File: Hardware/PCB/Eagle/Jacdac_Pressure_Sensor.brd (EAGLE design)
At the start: 33.8 x 27.9 mm, 30 parts, among them J1 JACDAC-CONNECTOR, J2 SWD-ADAPTER-, J3 HEADER_MALE-1X07, U1 NCP114ASN330T1G, U2 STM32F042F6P6, U3 BAT54S,235, U4 LPS33HWTR

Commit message: Updated design
Use I2C instead of SPI
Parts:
- J1: value JACDAC-CONNECTOR -> JACDAC_EDGE_CONN-INNIE; device milador:JACDAC-CONNECTOR -> Jacdac:JACDAC-EDGE-CONN-INNIE
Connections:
- removed net N$17: D3.2, FB1.2, J1.P3
- removed net SCK: J3.3, SJ1.1, U2.11, U4.2
- new net J_DATA: D3.2, FB1.2, J1.JD1, J1.JD2, J1.JD3
- new net SCL: J3.3, SJ1.1, U2.17, U4.2
- net GND: now also J1.GND1, J1.GND2, J1.GND3, J1.GND4; no longer J1.P2
- net SDA: now also U2.18; no longer U2.13
- net VCC: now also J1.VDD1, J1.VDD2, J1.VDD3; no longer J1.P1
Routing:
- net SCK: track 34.5 -> 0.00 mm, vias 2 -> 0
- net SCL: track 0.00 -> 29.8 mm, vias 0 -> 2
- net J_DATA: track 0.00 -> 20.4 mm
- net N$17: track 10.8 -> 0.00 mm
- net VCC: track 17.0 -> 24.0 mm
- net SDA: track 33.1 -> 29.1 mm
- net GND: track 14.6 -> 16.4 mm
- net RESET: track 13.1 -> 12.4 mm
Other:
- board size 33.8 x 27.9 mm -> 27.9 x 27.9 mm
- board text added: "SCL"
- board text removed: "SCK"

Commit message: Corrected Capacitor values
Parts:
- C5: value 33pF -> 1uF
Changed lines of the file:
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@@
 <attribute name="NAME" x="14.224" y="8.382" size="0.8128" layer="25" ratio="15" rot="R90" align="bottom-center"/>
 </element>
-<element name="C5" library="milador_SMD" library_urn="urn:adsk.eagle:library:27847482" package="0603" package3d_urn="urn:adsk.eagle:package:29222124/2" value="33pF" x="15.24" y="13.462" smashed="yes">
+<element name="C5" library="milador_SMD" library_urn="urn:adsk.eagle:library:27847482" package="0603" package3d_urn="urn:adsk.eagle:package:29222124/2" value="1uF" x="15.24" y="13.462" smashed="yes">
 <attribute name="NAME" x="12.8524" y="12.9286" size="0.8128" layer="25" font="vector" ratio="15" align="bottom-center"/>
 <attribute name="VALUE" x="13.0302" y="12.4968" size="0.8128" layer="27" font="vector" ratio="15" align="top-center"/>

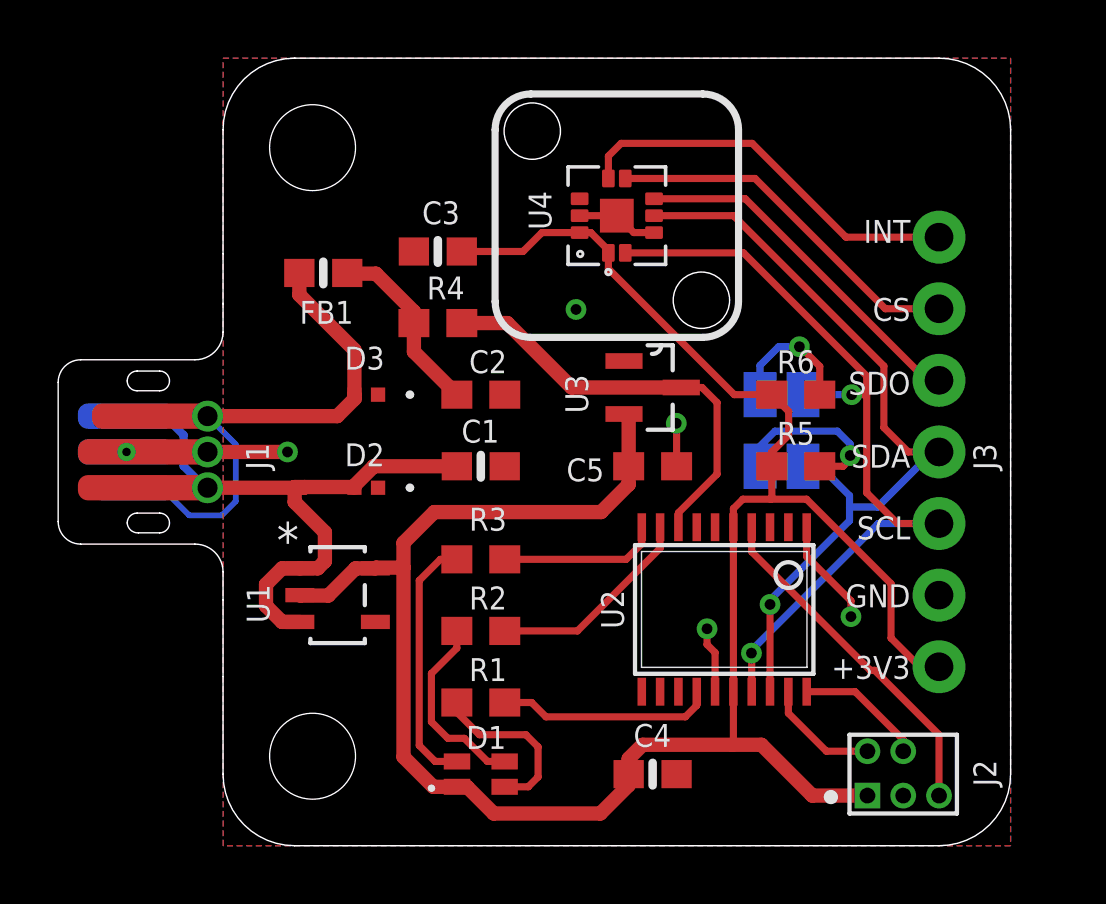
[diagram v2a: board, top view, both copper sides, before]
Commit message: Updated main design
Centering the sensor
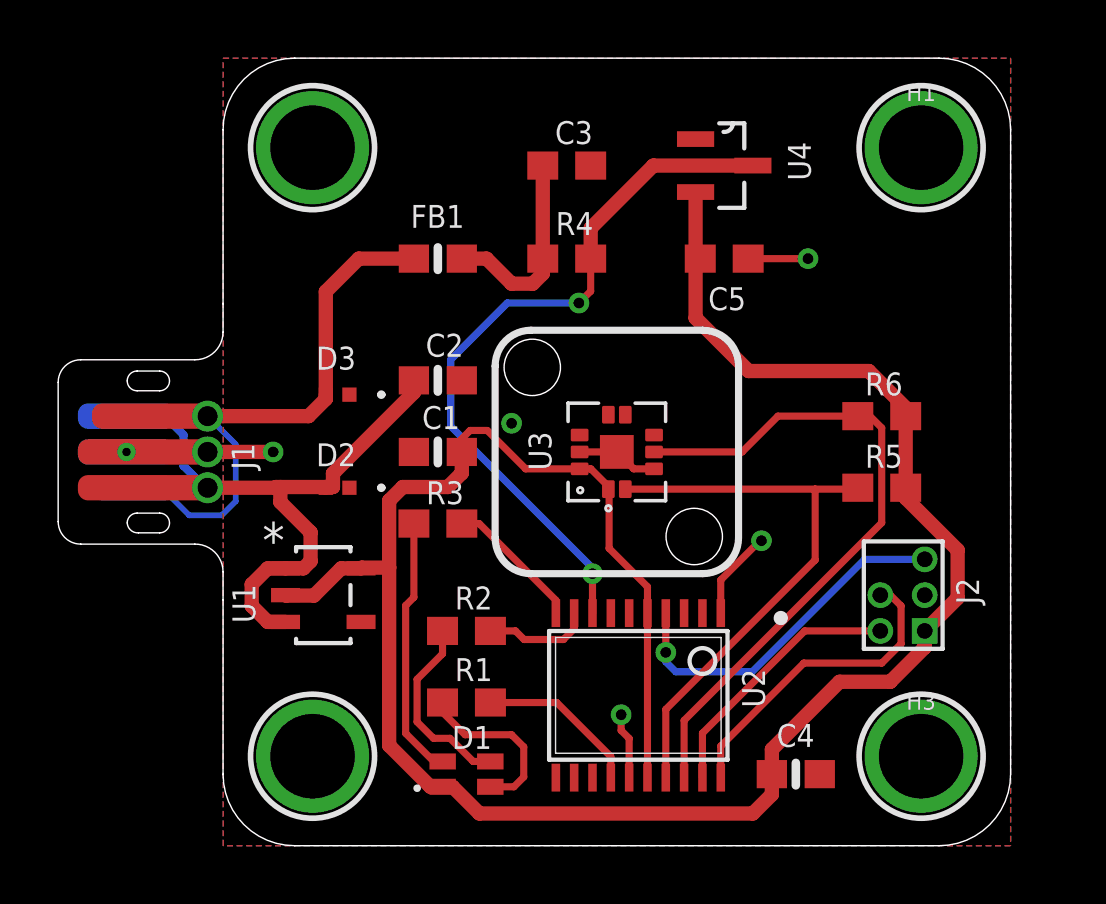
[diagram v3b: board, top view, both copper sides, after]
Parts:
- removed J3: HEADER_MALE-1X07, milador:HEADER_MALE-1X07
- removed SJ1, SJ2: (no value), milador_SMD:SOLDERJUMPER_CLOSEDWIRE
- removed U$1: MILADOR-PIN-NAME-SDA, milador:PIN-SDA
- removed U$2: MILADOR-PIN-NAME-SCK, milador:PIN-SCK
- added H1, H3: MOUNTINGHOLE3.0THIN, milador:MOUNTINGHOLE_3.0_PLATEDTHIN
- C1: value 1uF -> 0.1uF
- C2: value 33pF -> 1uF; device milador_SMD:0603 -> milador_SMD:0603-NO
- C3: value 0.1uF -> 33pF; device milador_SMD:0603-NO -> milador_SMD:0603
- H2, JP3: value STAND-OFF-3.0 -> MOUNTINGHOLE3.0THIN; device milador:STAND-OFF-3.0 -> milador:MOUNTINGHOLE_3.0_PLATEDTHIN
- U3: value BAT54S,235 -> LPS33HWTR; device milador_SMD:SOT23-3 -> milador_SMD:PQFN60P330X330X290-11N
- U4: value LPS33HWTR -> BAT54S,235; device milador_SMD:PQFN60P330X330X290-11N -> milador_SMD:SOT23-3
- moved C5 7.79 mm to (17.8, 20.8)
- moved J2 6.19 mm to (24.9, 7.62), turned to 90 degrees
- moved C3 5.49 mm to (12.2, 24.1), turned to 0 degrees
- moved R4 5.11 mm to (12.2, 20.8)
- moved C4 5.08 mm to (20.3, 2.54)
- moved U2 4.31 mm to (14.7, 5.33)
- moved U4 4.20 mm to (17.8, 24.1), turned to 0 degrees
- moved FB1 4.10 mm to (7.62, 20.8)
- moved R5 3.14 mm to (23.4, 12.7), turned to 0 degrees
- moved R6 3.14 mm to (23.4, 15.2), turned to 0 degrees
- moved U3 2.62 mm to (14.0, 14.0), turned to 90 degrees
- moved R3 1.98 mm to (7.62, 11.4)
- moved C2 1.61 mm to (7.62, 16.5)
- moved C1 1.61 mm to (7.62, 14.0), turned to 180 degrees
- moved D2 1.02 mm to (4.06, 12.7)
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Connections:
- removed net CS: J3.6, U4.6
- removed net INT: J3.7, U4.7
- removed net N$6: R6.1, SJ1.2
- removed net N$7: R5.1, SJ2.2
- removed net SDO: J3.5, U4.5
- net +3V3: now also C1.1, U3.1, U3.10, U4.2; no longer C3.1, J3.1, U3.2, U4.1, U4.10
- net GND: now also U3.3, U3.8, U3.9, U3.EP, U4.1; no longer J3.2, U3.1, U4.3, U4.8, U4.9, U4.EP
- net JD_DATA: now also U4.3; no longer U3.3
- net N$4: now also C3.1; no longer C2.1
- net SCL: now also R5.1, U3.2; no longer J3.3, SJ1.1, U4.2
- net SDA: now also R6.1, U3.4; no longer J3.4, SJ2.1, U4.4
- net VCC: now also C2.1; no longer C1.1
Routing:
- net INT: track 14.1 -> 0.00 mm
- net CS: track 13.0 -> 0.00 mm
- net SDO: track 12.8 -> 0.00 mm
- net JD_DATA: track 15.2 -> 26.0 mm, vias 0 -> 2
- net SCL: track 29.8 -> 20.7 mm, vias 2 -> 0
- net SWCLK: track 4.54 -> 11.3 mm
- net N$7: track 6.04 -> 0.00 mm, vias 1 -> 0
- net SWDIO: track 4.13 -> 9.39 mm
- net SDA: track 29.1 -> 24.1 mm, vias 1 -> 0
- net N$6: track 4.73 -> 0.00 mm, vias 1 -> 0
- net RGB_G: track 7.47 -> 3.81 mm
- net RGB_B: track 7.68 -> 5.81 mm
- net J_DATA: track 20.4 -> 21.5 mm
- net RGB_R: track 5.68 -> 4.92 mm
- net N$4: track 6.51 -> 7.22 mm
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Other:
- outline, holes or cut-outs redrawn
- board text removed: "+3V3"
- board text removed: "CS"
- board text removed: "GND"
- board text removed: "INT"
- board text removed: "SCL"
- board text removed: "SDA"
- board text removed: "SDO"

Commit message: Updated PCB
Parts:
- removed JP3: MOUNTINGHOLE3.0THIN, milador:MOUNTINGHOLE_3.0_PLATEDTHIN
- added H4: MOUNTINGHOLE2.5, milador:MOUNTINGHOLE_2.5_PLATED
- added MMC_LOGO: MMC_LOGO-SM, MMC Eagle:MMC_SMALL_LOGO
- added U$1: JACDAC-DEVICE-LPS33HW, milador:JACDAC-LPS33HW
- H1, H2, H3: value MOUNTINGHOLE3.0THIN -> MOUNTINGHOLE2.5; device milador:MOUNTINGHOLE_3.0_PLATEDTHIN -> milador:MOUNTINGHOLE_2.5_PLATED
- moved H1 30.5 mm to (3.17, 3.17)
- moved H3 21.6 mm to (24.8, 24.8)
- moved LABEL2 15.4 mm to (23.1, 18.6)
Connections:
- net GND: now also H3.P$1, H4.P$1
- net J_DATA: now also H2.P$1
- net VCC: now also H1.P$1
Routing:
- net VCC: track 23.9 -> 29.5 mm
- net J_DATA: track 21.5 -> 26.3 mm
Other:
- board text added: "5V"
- board text added: "GND"
- board text added: "JD"
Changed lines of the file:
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@@
 <setting verticaltext="up"/>
 </settings>
-<grid distance="0.001" unitdist="inch" unit="inch" style="lines" multiple="1" display="yes" altdistance="0.005" altunitdist="inch" altunit="inch"/>
+<grid distance="0.0006" unitdist="inch" unit="inch" style="lines" multiple="1" display="yes" altdistance="0.005" altunitdist="inch" altunit="inch"/>
 <layers>
 <layer number="1" name="Top" color="4" fill="1" visible="yes" active="yes"/>
@@
 </layers>
 <board>
-<fusionsync huburn="a.cGVyc29uYWw6dWUyYWQxOTI2" projecturn="a.cGVyc29uYWw6dWUyYWQxOTI2IzIwMjEwOTEzNDQzNTc2ODA2" f3durn="urn:adsk.wipprod:dm.lineage:uby1OiGsR5OmPWsZuNtneA" pcbguid="" lastpulledtime="" lastsyncedchangeguid="" latestrevisionid="4bb2a5f7-9195-4a02-b50d-8d35879bc375" lastsyncedrevisionid="4bb2a5f7-9195-4a02-b50d-8d35879bc375" lastboardhashguid="187e14e1-9a08-c98b-b799-0e1be3d56bf4" lastpushedtime="2021-09-18T05:05:42Z" linktopcb3d="true"/>
+<fusionsync huburn="a.cGVyc29uYWw6dWUyYWQxOTI2" projecturn="a.cGVyc29uYWw6dWUyYWQxOTI2IzIwMjEwOTEzNDQzNTc2ODA2" f3durn="urn:adsk.wipprod:dm.lineage:uby1OiGsR5OmPWsZuNtneA" pcbguid="" lastpulledtime="" lastsyncedchangeguid="" latestrevisionid="af606afd-fa91-40a1-9cdc-3a86e01ece8c" lastsyncedrevisionid="af606afd-fa91-40a1-9cdc-3a86e01ece8c" lastboardhashguid="dc86e965-abde-f830-b550-b611301090e1" lastpushedtime="2022-03-29T02:43:38Z" linktopcb3d="true"/>
 <plain>
 <wire x1="2.54" y1="27.94" x2="25.4" y2="27.94" width="0.05" layer="20"/>
@@
 <wire x1="9.652" y1="17.018" x2="10.922" y2="18.288" width="0.254" layer="21" curve="-90"/>
 <wire x1="10.922" y1="18.288" x2="17.018" y2="18.288" width="0.254" layer="21"/>
-<circle x="19.7866" y="8.0772" radius="0.127" width="0.254" layer="21"/>
-<circle x="19.7866" y="8.0772" radius="0.127" width="0.254" layer="22"/>
+<circle x="18.5674" y="7.1628" radius="0.127" width="0.254" layer="21"/>
+<circle x="18.5674" y="7.1628" radius="0.127" width="0.254" layer="21"/>
 <wire x1="22.733" y1="10.795" x2="22.733" y2="6.985" width="0.1524" layer="22"/>
 <wire x1="22.733" y1="6.985" x2="25.527" y2="6.985" width="0.1524" layer="22"/>
@@
 <wire x1="25.527" y1="6.985" x2="25.527" y2="10.795" width="0.1524" layer="21"/>
 <wire x1="25.527" y1="10.795" x2="22.733" y2="10.795" width="0.1524" layer="21"/>
+<circle x="24.9428" y="6.2484" radius="0.127" width="0.254" layer="21"/>
+<text x="0.7112" y="21.8948" size="0.8128" layer="21" ratio="15">JD</text>
+<text x="24.9936" y="21.5646" size="0.8128" layer="21" ratio="15">GND</text>
+<text x="0.6604" y="5.4864" size="0.8128" layer="21" ratio="15">5V</text>
+<text x="21.209" y="0.5334" size="0.8128" layer="21" ratio="15">GND</text>
 </plain>
 <attributes>
@@
 </autorouter>
 <elements>
-<element name="JP3" library="milador" library_urn="urn:adsk.eagle:library:12595918" package="MOUNTINGHOLE_3.0_PLATEDTHIN" package3d_urn="urn:adsk.eagle:package:29232285/1" value="MOUNTINGHOLE3.0THIN" x="3.175" y="3.175" smashed="yes">
+<element name="H1" library="milador" library_urn="urn:adsk.eagle:library:12595918" package="MOUNTINGHOLE_2.5_PLATED" package3d_urn="urn:adsk.eagle:package:29232281/2" value="MOUNTINGHOLE2.5" x="3.175" y="3.175" smashed="yes">
 <attribute name="BOM" value="EXCLUDE" x="3.175" y="3.175" size="1.778" layer="27" display="off"/>
 </element>
-<element name="H2" library="milador" library_urn="urn:adsk.eagle:library:12595918" package="MOUNTINGHOLE_3.0_PLATEDTHIN" package3d_urn="urn:adsk.eagle:package:29232285/1" value="MOUNTINGHOLE3.0THIN" x="3.175" y="24.765" smashed="yes">
+<element name="H2" library="milador" library_urn="urn:adsk.eagle:library:12595918" package="MOUNTINGHOLE_2.5_PLATED" package3d_urn="urn:adsk.eagle:package:29232281/2" value="MOUNTINGHOLE2.5" x="3.175" y="24.765" smashed="yes">
 <attribute name="BOM" value="EXCLUDE" x="3.175" y="24.765" size="1.778" layer="27" display="off"/>
 </element>
@@
 </element>
 <element name="LABEL3" library="milador" library_urn="urn:adsk.eagle:library:12595918" package="MILADOR_LOGO1" package3d_urn="urn:adsk.eagle:package:28431737/1" value="MILADOR-LOGO-" x="2.286" y="13.97" smashed="yes" rot="MR90"/>
-<element name="LABEL2" library="milador" library_urn="urn:adsk.eagle:library:12595918" package="JACDAC-PRESSURE-SENSOR" package3d_urn="urn:adsk.eagle:package:30748291/1" value="JACDAC-DEVICE-PS" x="8.3058" y="14.3256" smashed="yes" rot="MR90"/>
+<element name="LABEL2" library="milador" library_urn="urn:adsk.eagle:library:12595918" package="JACDAC-PRESSURE-SENSOR" package3d_urn="urn:adsk.eagle:package:30748291/2" value="JACDAC-DEVICE-PS" x="23.1038375" y="18.623278125" smashed="yes" rot="MR90"/>
 <element name="R5" library="milador_SMD" library_urn="urn:adsk.eagle:library:27847482" package="0603" package3d_urn="urn:adsk.eagle:package:29222124/2" value="4.7K" x="23.368" y="12.7" smashed="yes">
 <attribute name="NAME" x="23.4442" y="14.224" size="0.8128" layer="25" font="vector" ratio="15" rot="R180" align="bottom-center"/>
@@
 <attribute name="NAME" x="1.116" y="13.343" size="0.8128" layer="21" font="vector" ratio="15" rot="R90"/>
 </element>
-<element name="H1" library="milador" library_urn="urn:adsk.eagle:library:12595918" package="MOUNTINGHOLE_3.0_PLATEDTHIN" package3d_urn="urn:adsk.eagle:package:29232285/1" value="MOUNTINGHOLE3.0THIN" x="24.765" y="24.765" smashed="yes">
+<element name="H3" library="milador" library_urn="urn:adsk.eagle:library:12595918" package="MOUNTINGHOLE_2.5_PLATED" package3d_urn="urn:adsk.eagle:package:29232281/2" value="MOUNTINGHOLE2.5" x="24.765" y="24.765" smashed="yes">
 <attribute name="BOM" value="EXCLUDE" x="24.765" y="24.765" size="1.778" layer="27" display="off"/>
-<attribute name="NAME" x="24.765" y="26.416" size="0.6096" layer="25" font="vector" ratio="20" align="bottom-center"/>
-</element>
-<element name="H3" library="milador" library_urn="urn:adsk.eagle:library:12595918" package="MOUNTINGHOLE_3.0_PLATEDTHIN" package3d_urn="urn:adsk.eagle:package:29232285/1" value="MOUNTINGHOLE3.0THIN" x="24.765" y="3.175" smashed="yes">
+</element>
+<element name="H4" library="milador" library_urn="urn:adsk.eagle:library:12595918" package="MOUNTINGHOLE_2.5_PLATED" package3d_urn="urn:adsk.eagle:package:29232281/2" value="MOUNTINGHOLE2.5" x="24.765" y="3.175" smashed="yes">
 <attribute name="BOM" value="EXCLUDE" x="24.765" y="3.175" size="1.778" layer="27" display="off"/>
-<attribute name="NAME" x="24.765" y="4.826" size="0.6096" layer="25" font="vector" ratio="20" align="bottom-center"/>
-</element>
+</element>
+<element name="MMC_LOGO" library="MMC Eagle" library_urn="urn:adsk.eagle:library:13126479" package="MMC_SMALL_LOGO" package3d_urn="urn:adsk.eagle:package:33611713/1" value="MMC_LOGO-SM" x="11.684" y="13.97" smashed="yes" rot="MR90"/>
+<element name="U$1" library="milador" library_urn="urn:adsk.eagle:library:12595918" package="JACDAC-LPS33HW" package3d_urn="urn:adsk.eagle:package:34994332/2" value="JACDAC-DEVICE-LPS33HW" x="18.669" y="19.796759375" smashed="yes" rot="MR90"/>
 </elements>
 <signals>
@@
 <wire x1="19.05" y1="10.8204" x2="19.1008" y2="10.8204" width="0.254" layer="1"/>
 <wire x1="19.05" y1="10.8204" x2="17.657" y2="9.4274" width="0.254" layer="1"/>
+<contactref element="H3" pad="P$1"/>
+<contactref element="H4" pad="P$1"/>
 </signal>
 <signal name="VCC">
@@
 <wire x1="-0.55" y1="12.7" x2="1.8542" y2="12.7" width="0.508" layer="1"/>
 <wire x1="1.8542" y1="12.7" x2="1.8796" y2="12.7254" width="0.508" layer="1"/>
+<contactref element="H1" pad="P$1"/>
+<wire x1="3.175" y1="3.175" x2="3.175" y2="7.5692" width="0.508" layer="1"/>
+<wire x1="2.8042" y1="7.94" x2="2.21615" y2="7.94" width="0.508" layer="1"/>
+<wire x1="3.175" y1="7.5692" x2="2.8042" y2="7.94" width="0.508" layer="1"/>
 </signal>
 <signal name="J_DATA">
 <contactref element="FB1" pad="2"/>
-<wire x1="6.77" y1="20.828" x2="4.8142" y2="20.828" width="0.508" layer="1"/>
-<wire x1="4.8142" y1="20.828" x2="3.6449" y2="19.6587" width="0.508" layer="1"/>
-<wire x1="3.6449" y1="19.6587" x2="3.6449" y2="16.002" width="0.508" layer="1"/>
 <wire x1="3.6449" y1="16.002" x2="3.6449" y2="15.8496" width="0.508" layer="1"/>
 <contactref element="D3" pad="2"/>
@@
 <wire x1="3.0353" y1="15.24" x2="-0.55" y2="15.24" width="0.508" layer="1"/>
 <wire x1="3.6449" y1="15.8496" x2="3.0353" y2="15.24" width="0.508" layer="1"/>
+<contactref element="H2" pad="P$1"/>
+<wire x1="3.6449" y1="24.2951" x2="3.175" y2="24.765" width="0.508" layer="1"/>
+<wire x1="3.6449" y1="16.002" x2="3.6449" y2="20.828" width="0.508" layer="1"/>
+<wire x1="3.6449" y1="20.828" x2="3.6449" y2="24.2951" width="0.508" layer="1"/>
+<wire x1="6.77" y1="20.828" x2="3.6449" y2="20.828" width="0.508" layer="1"/>
 </signal>
 <signal name="+3V3">
@@
 <wire x1="15.29" y1="13.97" x2="18.415" y2="13.97" width="0.254" layer="1"/>
 <wire x1="18.415" y1="13.97" x2="19.685" y2="15.24" width="0.254" layer="1"/>
-<wire x1="23.368" y1="11.4554" x2="16.357" y2="4.4444" width="0.254" layer="1"/>
+<wire x1="23.368" y1="11.4554" x2="19.8882" y2="7.9756" width="0.254" layer="1"/>
+<wire x1="19.8882" y1="7.9756" x2="16.357" y2="4.4444" width="0.254" layer="1"/>
 <wire x1="23.368" y1="14.8218" x2="22.9498" y2="15.24" width="0.254" layer="1"/>
 <wire x1="22.9498" y1="15.24" x2="22.518" y2="15.24" width="0.254" layer="1"/>
